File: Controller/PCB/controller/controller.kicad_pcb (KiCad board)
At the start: 2 copper layers, 70 parts, among them J1 nRF24L01_Conn, J2 SERIAL_DEBUG_CONNECTOR, Q1 S9013, Q2 S9013, Q3 S9013, Q4 S9013, Q5 S9013, U1 Joystick, U2 Joystick, U3 NLAS4684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

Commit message: Update Symbol Library
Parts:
- A1: footprint Module:Arduino_Nano -> My_library:NUCELO-L432KC_SMD
- BT1, BT2: moved to B.Cu
- moved BZ1 120.3 mm to (9.11, -7.83)
- moved Btn_2 120.3 mm to (138.8, -38.1)
- moved Btn_3 120.3 mm to (149.9, -38.1)
- moved Btn_5 120.3 mm to (127.8, -38.1)
- moved C1 120.3 mm to (47.4, -1.29)
- moved C2 120.3 mm to (55.4, -3.31)
- moved C3 120.3 mm to (61.4, -10.8)
- moved C4 120.3 mm to (59.4, -3.31)
- moved C5 120.3 mm to (114.2, -46.7)
- moved C7 120.3 mm to (77.4, -10.8)
- moved C8 120.3 mm to (63.4, -5.82)
- moved D1 120.3 mm to (13.1, 4.69)
- moved D2 120.3 mm to (38.6, -5.06)
- moved D3 120.3 mm to (30.0, 1.53)
- moved D4 120.3 mm to (47.4, -8.86)
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
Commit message: Minor Schematic Updates
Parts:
- J2: footprint Connector_PinHeader_2.54mm:PinHeader_2x03_P2.54mm_Vertical_SMD -> Connector_PinHeader_2.54mm:PinHeader_2x05_P2.54mm_Vertical_SMD
- moved J2 30.9 mm to (27.9, 30.5)
- moved A1 20.5 mm to (148.5, 106.7), turned to 180 degrees
- moved C5 6.57 mm to (111.8, -40.6)
- moved R26 6.46 mm to (111.8, -50.8)
- moved R3 4.18 mm to (111.8, -45.7)
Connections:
- J2 pad 1: DEBUG -> DEBUG_IRQ
- J2 pad 2: NRF_SCK -> DEBUG_MOSI
- J2 pad 3: DEBUG_MISO -> DEBUG
- J2 pad 4: DEBUG_IRQ -> +3V3
- J2 pad 5: DEBUG_MOSI -> NRF_SCK
- J2 pad 6: +3V3 -> DEBUG_MISO

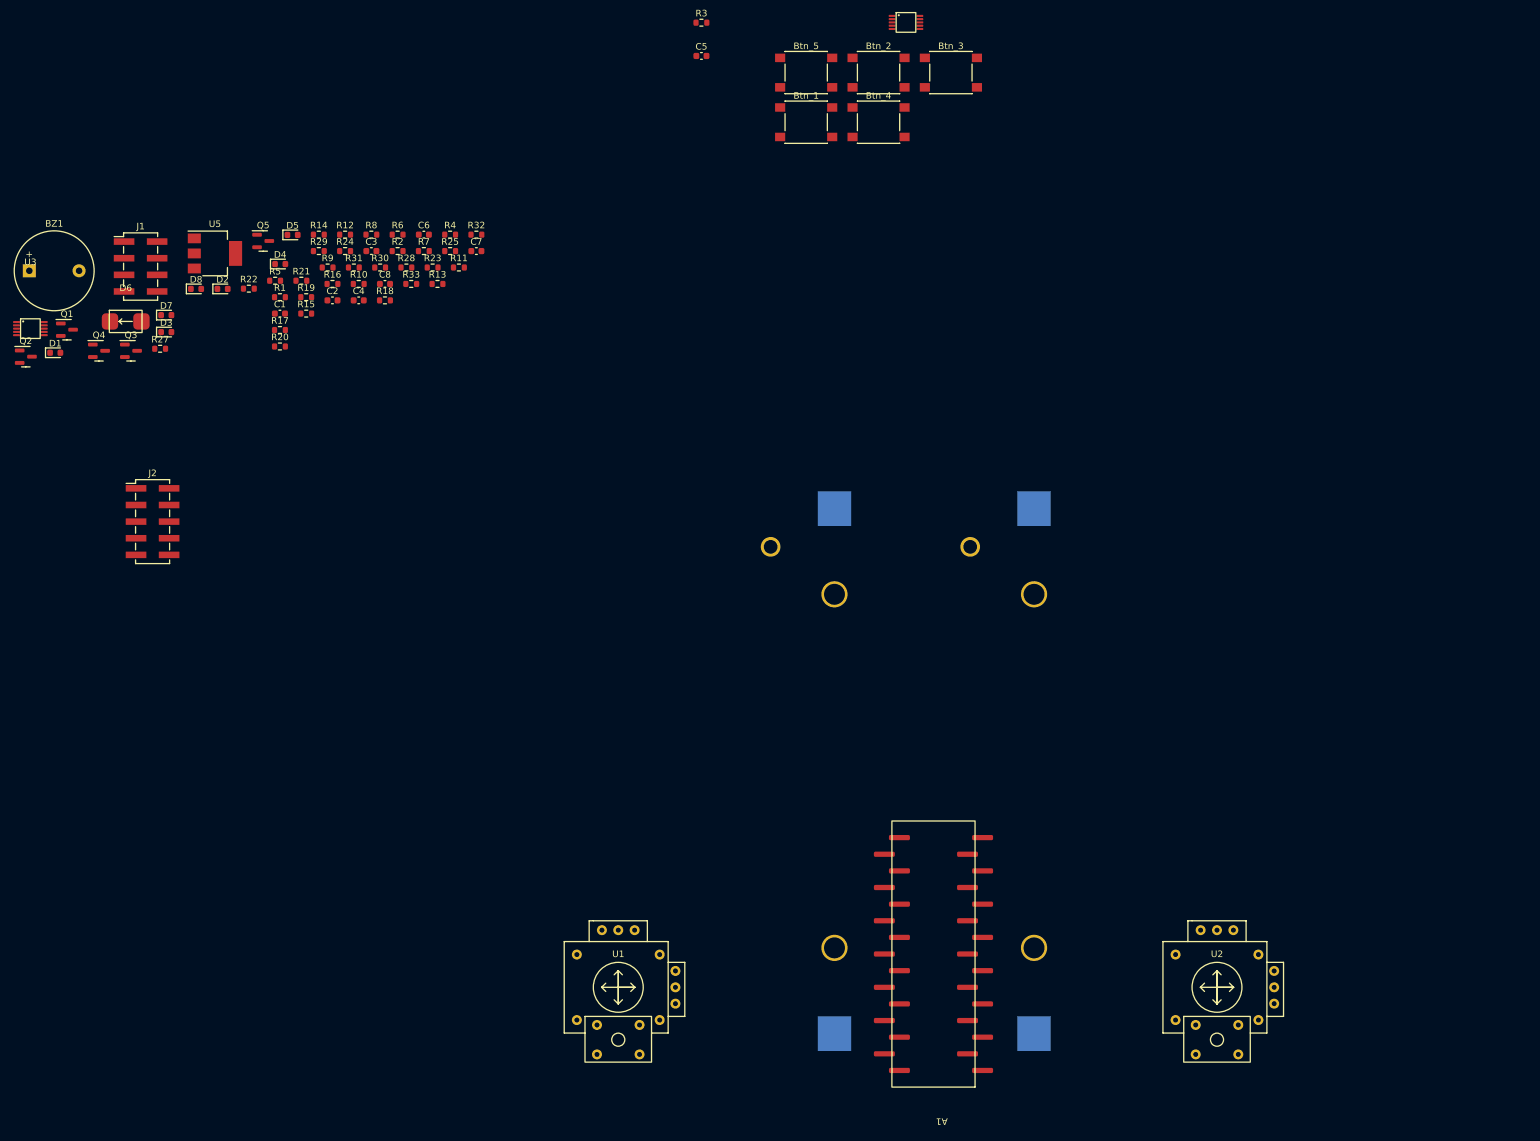
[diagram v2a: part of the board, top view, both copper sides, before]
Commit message: Update Schematic and Continue to work on Cpp
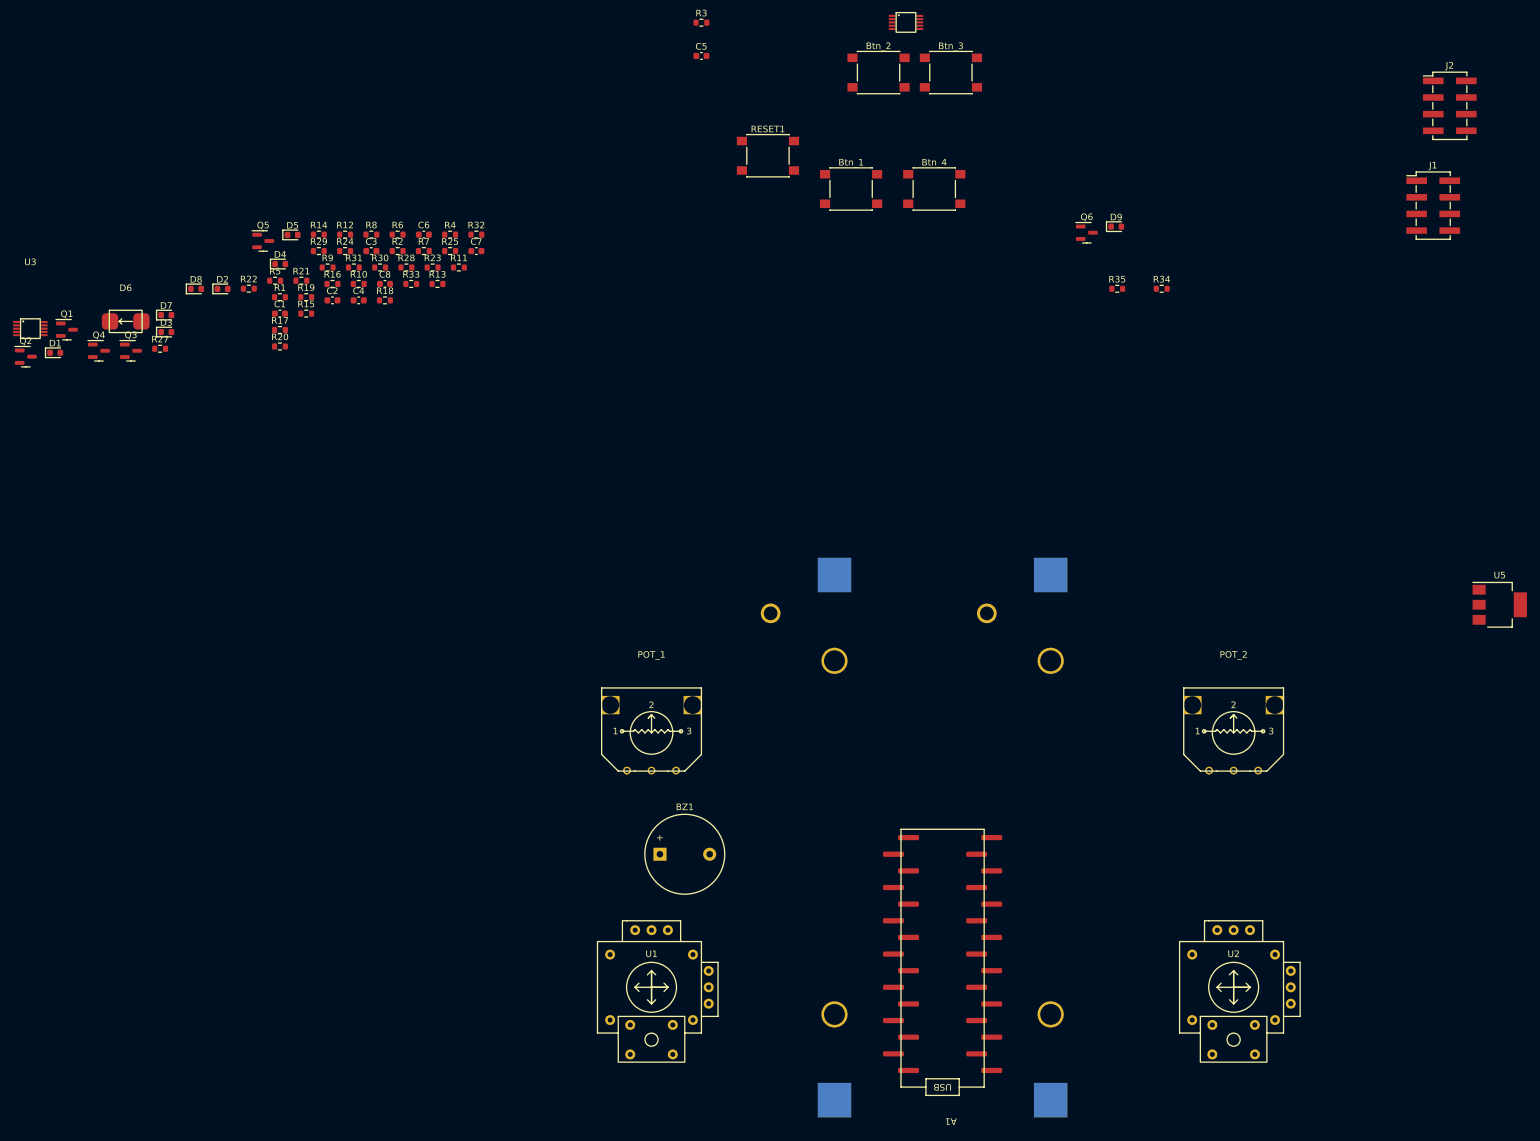
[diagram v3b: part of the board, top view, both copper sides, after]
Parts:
- added D9: RED, LED_SMD:LED_0603_1608Metric, F.Cu at (175.1, -14.6)
- added POT_1: R_POT, My_library:PDB12 Series, F.Cu at (104.1, 63.5)
- added POT_2: R_POT, My_library:PDB12 Series, F.Cu at (193.0, 63.5)
- added Q6: S9013, Package_TO_SOT_SMD:SOT-23, F.Cu at (170.6, -13.6)
- added R34: 4K7, Resistor_SMD:R_0603_1608Metric, F.Cu at (182.1, -5.08)
- added R35: 1K, Resistor_SMD:R_0603_1608Metric, F.Cu at (175.3, -5.08)
- D1, D4: value LED -> RED
- D2, D5, D7, D8: value LED -> BLUE
- D3: value LED -> GREEN
- J2: value SERIAL_DEBUG_CONNECTOR -> SERIAL_DEBUG_Conn; footprint Connector_PinHeader_2.54mm:PinHeader_2x05_P2.54mm_Vertical_SMD -> Connector_PinHeader_2.54mm:PinHeader_2x04_P2.54mm_Vertical_SMD
- R25, R31, R33: value 1K -> 390R
- R27, R29: value 1K -> 2K
- moved J2 208.0 mm to (226.1, -33.0)
- moved U5 203.4 mm to (233.7, 43.2)
- moved J1 197.6 mm to (223.5, -17.8)
- moved BZ1 131.2 mm to (105.4, 81.3)
- moved RESET1 14.0 mm to (121.9, -25.4)
- moved Btn_4 13.3 mm to (147.3, -20.3)
- moved Btn_1 12.3 mm to (134.6, -20.3)
- moved BT1 10.5 mm to (165.1, 78.7)
- moved BT2 10.2 mm to (132.1, 78.7)
- moved U1 5.08 mm to (104.1, 101.6)
- moved U2 2.54 mm to (193.0, 101.6)
- moved A1 1.39 mm to (149.9, 106.7)
- renumbered Btn_5 to RESET1
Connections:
- J1 pad 2: NRF_CE -> +3V3
- J1 pad 3: NRF_SCK -> NRF_CE
- J1 pad 4: NRF_MISO -> NRF_CSN
- J1 pad 5: NRF_IRQ -> NRF_SCK
- J1 pad 7: NRF_CSN -> NRF_MISO
- J1 pad 8: +3V3 -> NRF_IRQ
- J2 pad 1: DEBUG_IRQ -> DEBUG
- J2 pad 2: DEBUG_MOSI -> +3V3
- J2 pad 3: DEBUG -> NRF_SCK
- J2 pad 4: +3V3 -> DEBUG_MOSI
- J2 pad 5: NRF_SCK -> DEBUG_MISO
- J2 pad 6: DEBUG_MISO -> DEBUG_IRQ
- J2 pad 7: DEBUG_IRQ -> +3V3
- J2 pad 8: DEBUG_MOSI -> DEBUG_WRONG_WAY

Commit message: Finalise Circuit Schematic
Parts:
- removed Btn_4: SW_SPST, Button_Switch_SMD:SW_Push_1P1T_NO_6x6mm_H9.5mm
- removed D3: GREEN, LED_SMD:LED_0603_1608Metric
- removed D8: BLUE, LED_SMD:LED_0603_1608Metric
- removed D9: RED, LED_SMD:LED_0603_1608Metric
- removed J2: SERIAL_DEBUG_Conn, Connector_PinHeader_2.54mm:PinHeader_2x04_P2.54mm_Vertical_SMD
- removed POT_1, POT_2: R_POT, My_library:PDB12 Series
- removed Q3, Q5, Q6: S9013, Package_TO_SOT_SMD:SOT-23
- removed R17, R22, R35: 1K, Resistor_SMD:R_0603_1608Metric
- removed R18, R20, R23: 10K, Resistor_SMD:R_0603_1608Metric
- removed R25, R33: 390R, Resistor_SMD:R_0603_1608Metric
- removed R27: 2K, Resistor_SMD:R_0603_1608Metric
- removed R32, R34: 4K7, Resistor_SMD:R_0603_1608Metric
- removed R7, R8: 620, Resistor_SMD:R_0603_1608Metric
- removed U4: NLAS4684, My_library:NLAS4684
- added C10: 10uF, Capacitor_SMD:CP_Elec_4x5.4, F.Cu at (150.5, 91.1)
- added C11: 10uF, Capacitor_SMD:CP_Elec_4x5.4, F.Cu at (133.5, 106.6)
- added C12: 100nF, Capacitor_SMD:C_0603_1608Metric, F.Cu at (179.9, 65.4)
- added C13: 100nF, Capacitor_SMD:C_0603_1608Metric, F.Cu at (202.6, 42.6)
- added C9: 10uF, Capacitor_SMD:CP_Elec_4x5.4, F.Cu at (191.8, 41.7)
- added SW1: SW_SPDT, My_library:KNX-1-D1, F.Cu at (105.2, 118.5)
- BT1, BT2: moved to F.Cu
- BZ1: footprint Buzzer_Beeper:Buzzer_12x9.5RM7.6 -> My_library:Buzzer
- C1: value 100nF -> 10uF; footprint Capacitor_SMD:C_0603_1608Metric -> Capacitor_SMD:CP_Elec_4x5.4
- D2: value BLUE -> 1N5817; footprint LED_SMD:LED_0603_1608Metric -> My_library:1N5817M
- U3: value NLAS4684 -> LM2940-3.0; footprint My_library:NLAS4684 -> Package_TO_SOT_SMD:SOT-223
- moved Q2 192.9 mm to (198.1, 41.0)
- moved U3 179.5 mm to (181.8, 50.5)
- moved Q4 175.8 mm to (190.4, 46.9)
- moved Q1 172.5 mm to (178.1, 56.9)
- moved R26 166.9 mm to (121.5, 115.8)
- moved D1 165.6 mm to (167.9, 63.5)
- moved J1 157.7 mm to (123.2, 103.9)
- moved R5 157.1 mm to (194.8, 45.9)
- moved D7 153.3 mm to (167.9, 66.1)
- moved R1 151.3 mm to (188.7, 50.4)
- moved D6 148.5 mm to (120.9, 112.3)
- moved R14 148.0 mm to (125.5, 115.8)
- moved R15 146.8 mm to (186.6, 55.9)
- moved D2 144.7 mm to (115.3, 117.7)
- moved D5 144.7 mm to (171.9, 63.5)
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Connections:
- A1 pad 1: LED_2 -> Btn_1
- A1 pad 10: SW_2 -> unconnected-(A1-Pad10)
- A1 pad 11: SERIAL_IRQ -> unconnected-(A1-Pad11)
- A1 pad 12: NRF_CE -> NRF_IRQ
- A1 pad 13: NRF_SCK -> SERIAL_MISO
- A1 pad 14: SERIAL_MOSI -> NRF_CE
- A1 pad 15: SERIAL_MISO -> NRF_CSN
- A1 pad 16: NRF_CSN -> NRF_SCK
- A1 pad 19: unconnected-(A1-Pad19) -> L_PITCH
- A1 pad 20: BUZZER -> L_ROLL
- A1 pad 21: POT_1 -> Btn_3
- A1 pad 22: POT_2 -> R_PITCH
- A1 pad 24: R_PITCH -> unconnected-(A1-Pad24)
- A1 pad 25: L_ROLL -> unconnected-(A1-Pad25)
- A1 pad 26: L_PITCH -> unconnected-(A1-Pad26)
- A1 pad 28: RESET -> unconnected-(A1-Pad28)
- A1 pad 3: unconnected-(A1-Pad3) -> RESET
- A1 pad 5: Btn_1 -> SERIAL_MOSI
- A1 pad 6: Btn_2 -> SW_1
- A1 pad 7: Btn_3 -> unconnected-(A1-Pad7)
- A1 pad 8: Btn_4 -> BUZZER
- A1 pad 9: SW_1 -> Btn_2
- C1 pad 1: Net-(C1-Pad1) -> +3V3
- C2 pad 1: Net-(C2-Pad1) -> +BATT
- D2 pad 1: Net-(D2-Pad1) -> +BATT
- D2 pad 2: Net-(D2-Pad2) -> Earth
- U3 pad 1: +5V -> Earth
- U3 pad 2: DEBUG_MOSI -> +3V3
- U3 pad 3: SERIAL_MOSI -> +BATT
- U3 pad 4: Net-(Q3-Pad1) -> (no net)

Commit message: Add power switch
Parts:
- added PWR_SW1: SW_SPDT, My_library:KNX-1-D1, F.Cu at (123.2, 34.3)
- BT1, BT2: moved to B.Cu
- moved Btn_2 134.5 mm to (37.1, 33.1)
- moved C12 134.5 mm to (45.7, 55.9)
- moved C13 134.5 mm to (68.3, 33.1)
- moved C3 134.5 mm to (47.5, 50.9)
- moved C4 134.5 mm to (41.6, 59.1)
- moved R1 134.5 mm to (54.5, 40.9)
- moved R13 134.5 mm to (48.4, 46.4)
- moved R2 134.5 mm to (54.5, 43.4)
- moved R28 134.5 mm to (68.3, 30.6)
- moved R3 134.5 mm to (37.7, 56.6)
- moved R30 134.5 mm to (45.7, 53.4)
- moved R5 134.5 mm to (60.6, 36.4)
- moved Btn_1 134.5 mm to (48.2, 33.1)
- moved C5 134.5 mm to (37.6, 59.2)
- moved C6 134.5 mm to (37.6, 61.7)
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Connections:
- C2 pad 1: +BATT -> BAT_PWR
- C7 pad 1: +BATT -> BAT_PWR
- D2 pad 1: +BATT -> BAT_PWR
- D6 pad 1: +BATT -> BAT_PWR
- U3 pad 3: +BATT -> BAT_PWR
- U5 pad 3: +BATT -> BAT_PWR

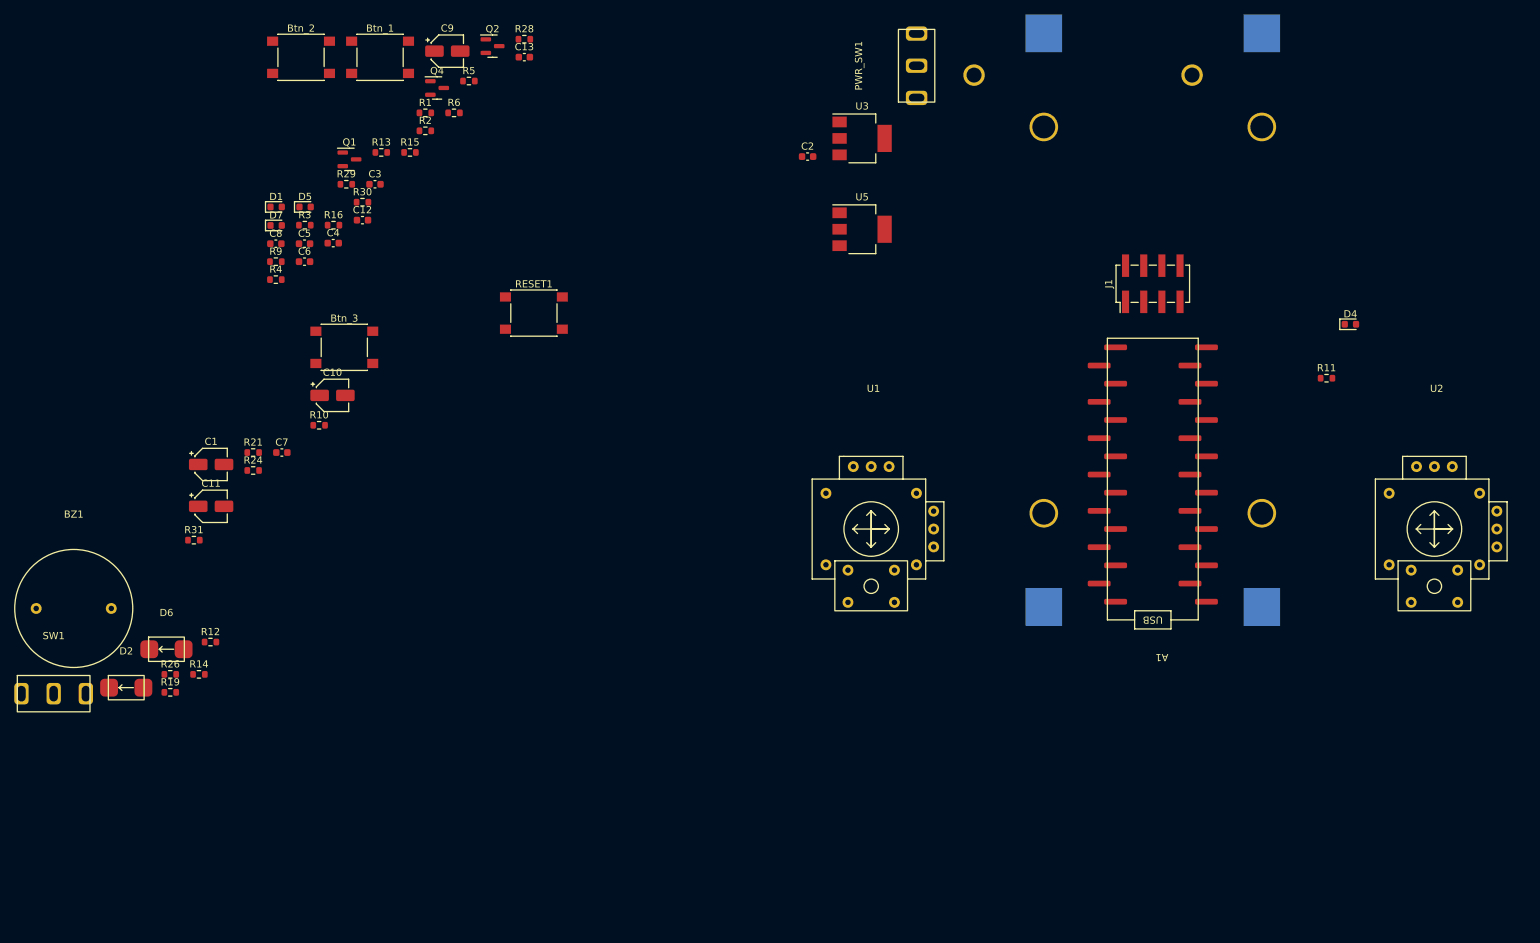
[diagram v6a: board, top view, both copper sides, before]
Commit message: Place Components on the PCB
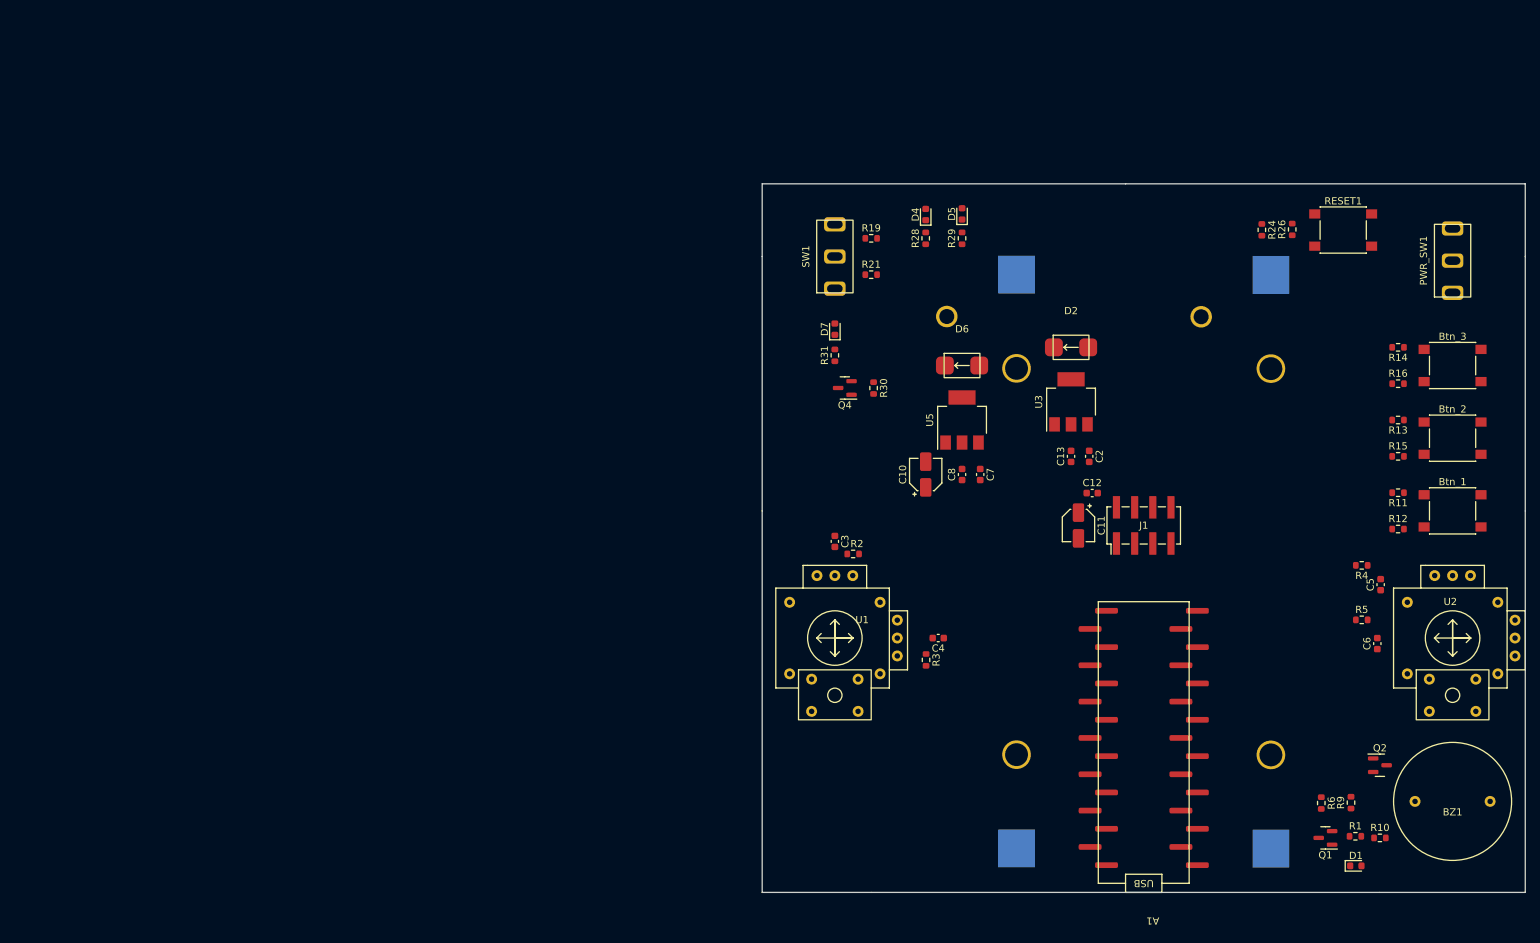
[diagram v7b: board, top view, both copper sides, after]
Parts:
- removed C1, C9: 10uF, Capacitor_SMD:CP_Elec_4x5.4
- moved BZ1 194.6 mm to (198.1, 137.1), turned to 180 degrees
- moved D1 176.8 mm to (184.6, 146.1)
- moved R14 173.8 mm to (190.5, 73.7), turned to 180 degrees
- moved Btn_2 169.6 mm to (198.1, 86.4)
- moved R26 168.7 mm to (175.7, 57.2), turned to 90 degrees
- moved R9 168.3 mm to (183.9, 137.3), turned to 90 degrees
- moved R12 166.8 mm to (190.5, 99.1)
- moved Q1 166.2 mm to (180.3, 142.2), turned to 180 degrees
- moved R1 164.7 mm to (184.5, 142.0)
- moved Btn_1 162.8 mm to (198.1, 96.5)
- moved Q2 159.7 mm to (188.0, 132.1)
- moved C6 159.2 mm to (187.6, 115.1), turned to 90 degrees
- moved R10 159.1 mm to (188.0, 142.2)
- moved C5 157.8 mm to (188.1, 106.8), turned to 90 degrees
- moved R4 157.0 mm to (185.4, 104.1), turned to 180 degrees
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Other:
- board outline added: 106.7 x 99.1 mm
